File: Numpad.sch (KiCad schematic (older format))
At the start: 35 parts, among them SW1 SW_PUSH, SW10 SW_PUSH, SW11 SW_PUSH, SW12 SW_PUSH, SW13 SW_PUSH, SW14 SW_PUSH, SW15 SW_PUSH, SW16 SW_PUSH, SW17 SW_PUSH, SW2 SW_PUSH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

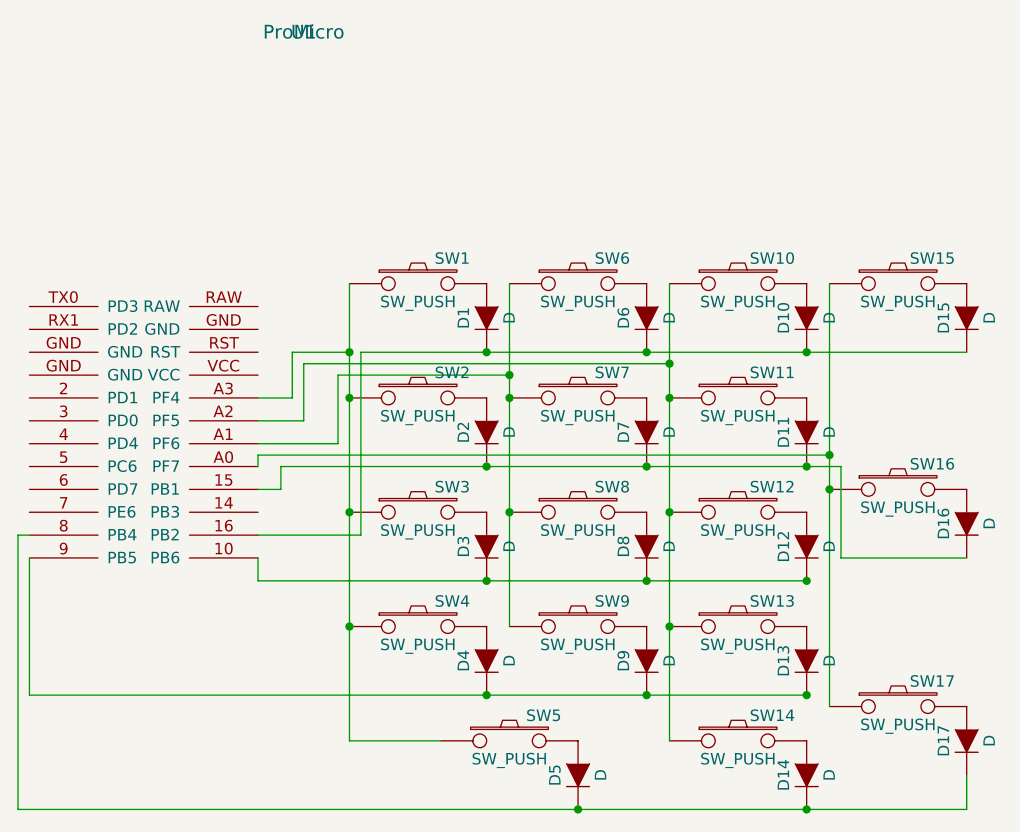
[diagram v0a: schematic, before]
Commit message: rotated diodes in the schematic. put the switches in the right places
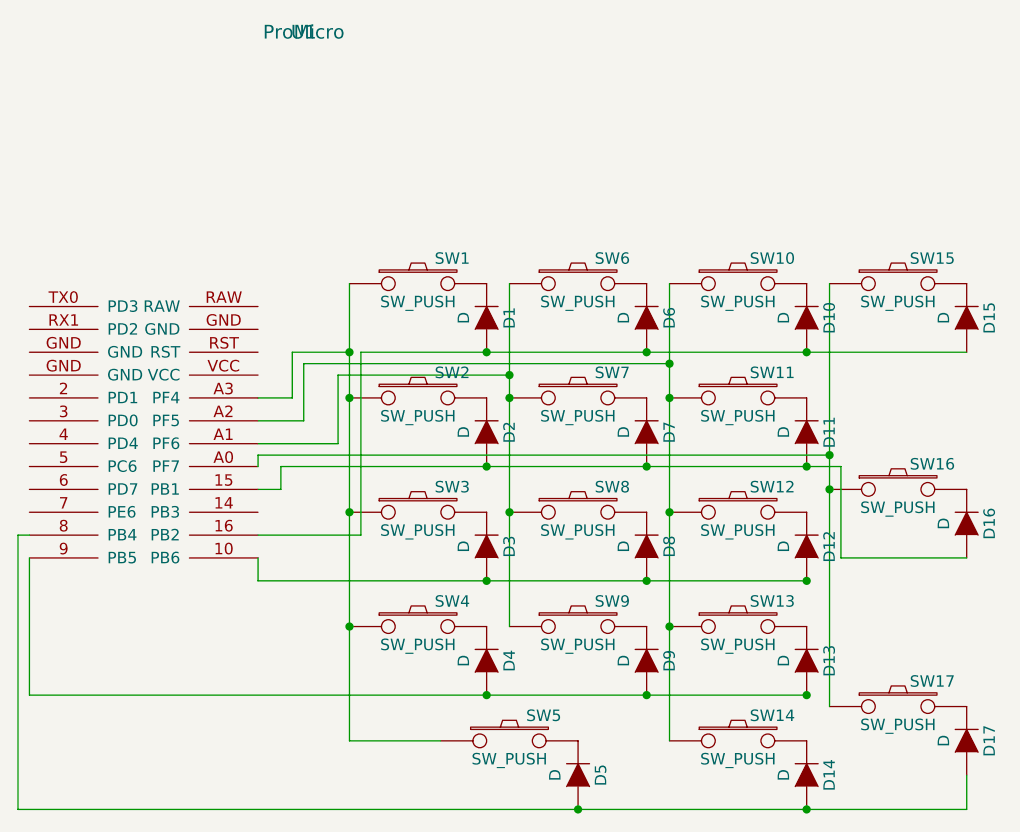
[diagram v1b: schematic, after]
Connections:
- net at SW6.2: now also D6.1 (K); no longer D6.2 (A)
- net at D1.2 (A): now also D10.2 (A), D15.2 (A), D6.2 (A), U1.16 (PB2); no longer SW1.2
- net at SW15.2: now also D15.1 (K); no longer D15.2 (A)
- net at SW10.2: now also D10.1 (K); no longer D10.2 (A)
- net at SW7.2: now also D7.1 (K); no longer D7.2 (A)
- net at D2.2 (A): now also D11.2 (A), D16.2 (A), D7.2 (A), U1.15 (PB1); no longer SW2.2
- net at SW11.2: now also D11.1 (K); no longer D11.2 (A)
- net at SW8.2: now also D8.1 (K); no longer D8.2 (A)
- net at D3.2 (A): now also D12.2 (A), D8.2 (A), U1.10 (PB6); no longer SW3.2
- net at SW12.2: now also D12.1 (K); no longer D12.2 (A)
- net at SW9.2: now also D9.1 (K); no longer D9.2 (A)
- net at D4.2 (A): now also D13.2 (A), D9.2 (A), U1.9 (PB5); no longer SW4.2
- net at SW13.2: now also D13.1 (K); no longer D13.2 (A)
- net at SW14.2: now also D14.1 (K); no longer D14.2 (A)
- net at D5.2 (A): now also D14.2 (A), D17.2 (A), U1.8 (PB4); no longer SW5.2
- net at SW17.2: now also D17.1 (K); no longer D17.2 (A)
- net at SW16.2: now also D16.1 (K); no longer D16.2 (A)
- new net: D1.1 (K), SW1.2
- new net: D2.1 (K), SW2.2
- new net: D3.1 (K), SW3.2
- new net: D4.1 (K), SW4.2
- new net: D5.1 (K), SW5.2
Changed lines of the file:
@@
 LIBS:contrib
 LIBS:valves
-LIBS:microchip_pic12mcu
-LIBS:freetronics_schematic
-LIBS:ArduProMiniTKB
-LIBS:Numpad-cache
+LIBS:splanck throughhole-cache
 EELAYER 25 0
 EELAYER END
@@
 F 3 "" H 4000 3450 60  0000 C CNN
 	1    4000 3450
-	0    -1   -1   0
+	0    1    1    0
 $EndComp
 $Comp
@@
 F 3 "" H 3300 3450 60  0000 C CNN
 	1    3300 3450
-	0    -1   -1   0
+	0    1    1    0
 $EndComp
 $Comp
@@
 F 3 "" H 5400 3450 60  0000 C CNN
 	1    5400 3450
-	0    -1   -1   0
+	0    1    1    0
 $EndComp
 $Comp
@@
 F 3 "" H 4700 3450 60  0000 C CNN
 	1    4700 3450
-	0    -1   -1   0
+	0    1    1    0
 $EndComp
 Wire Wire Line
@@
 F 3 "" H 4000 3950 60  0000 C CNN
 	1    4000 3950
-	0    -1   -1   0
+	0    1    1    0
 $EndComp
 $Comp
@@
 F 3 "" H 3300 3950 60  0000 C CNN
 	1    3300 3950
-	0    -1   -1   0
+	0    1    1    0
 $EndComp
 $Comp
@@
 F 3 "" H 4700 3950 60  0000 C CNN
 	1    4700 3950
-	0    -1   -1   0
+	0    1    1    0
 $EndComp
 Connection ~ 4700 4100
@@
 F 3 "" H 4000 4450 60  0000 C CNN
 	1    4000 4450
-	0    -1   -1   0
+	0    1    1    0
 $EndComp
 $Comp
@@
 F 3 "" H 3300 4450 60  0000 C CNN
 	1    3300 4450
-	0    -1   -1   0
+	0    1    1    0
 $EndComp
 $Comp
@@
 F 3 "" H 4700 4450 60  0000 C CNN
 	1    4700 4450
-	0    -1   -1   0
+	0    1    1    0
 $EndComp
 Connection ~ 4700 4600
@@
 F 3 "" H 4000 4950 60  0000 C CNN
 	1    4000 4950
-	0    -1   -1   0
+	0    1    1    0
 $EndComp
 $Comp
@@
 F 3 "" H 3300 4950 60  0000 C CNN
 	1    3300 4950
-	0    -1   -1   0
+	0    1    1    0
 $EndComp
 $Comp
@@
 F 3 "" H 4700 4950 60  0000 C CNN
 	1    4700 4950
-	0    -1   -1   0
+	0    1    1    0
 $EndComp
 Connection ~ 4700 5100
@@
 F 3 "" H 4700 5450 60  0000 C CNN
 	1    4700 5450
-	0    -1   -1   0
+	0    1    1    0
 $EndComp
 $Comp
@@
 F 3 "" H 3700 5450 60  0000 C CNN
 	1    3700 5450
-	0    -1   -1   0
+	0    1    1    0
 $EndComp
 $Comp
@@
 F 3 "" H 5400 5300 60  0000 C CNN
 	1    5400 5300
-	0    -1   -1   0
+	0    1    1    0
 $EndComp
 $Comp
@@
 F 3 "" H 5400 4350 60  0000 C CNN
 	1    5400 4350
-	0    -1   -1   0
+	0    1    1    0
 $EndComp
 Wire Wire Line
